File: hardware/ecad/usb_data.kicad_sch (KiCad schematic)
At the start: 4 parts, among them J6 Conn_01x04, U6 TS3USB30EDGSR

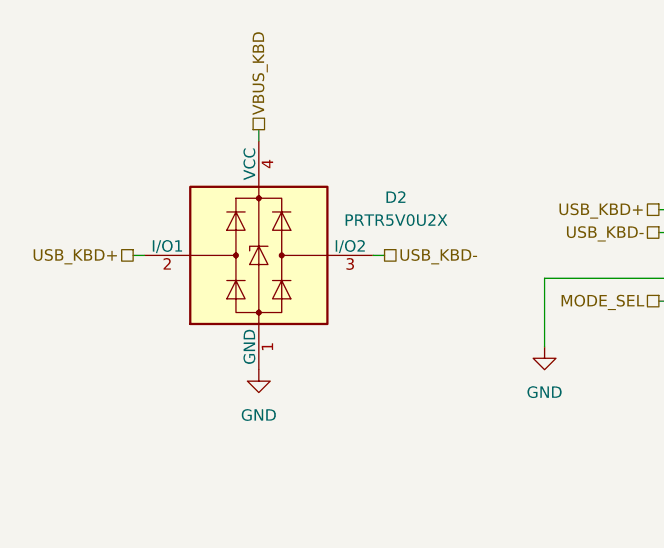
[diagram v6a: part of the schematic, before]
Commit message: Fixed minor errors and smaller issues withing schematics, moved v1 pcb and specific projet artifacts to archive. Updated changelog and finsihed pcb fopr version 2
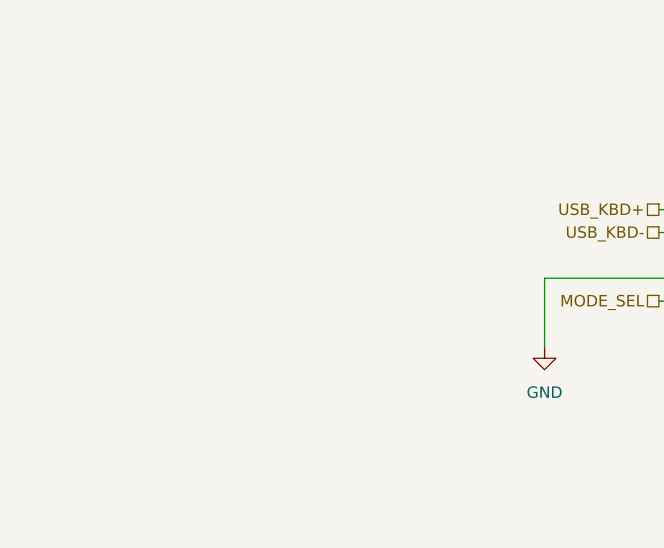
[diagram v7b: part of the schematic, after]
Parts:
- removed D2: PRTR5V0U2X, Package_TO_SOT_SMD:SOT-143, symbol Power_Protection:PRTR5V0U2X
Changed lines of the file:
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@@
-	(wire
-		(pts
-			(xy 99.06 101.6) (xy 100.33 101.6)
-		)
-		(stroke
-			(width 0)
-			(type default)
-		)
-	)
-	(wire
-		(pts
-			(xy 113.03 88.9) (xy 113.03 87.63)
-		)
-		(stroke
-			(width 0)
-			(type default)
-		)
-	)
 	(wire
 		(pts
@@
 		(pts
 			(xy 179.07 99.06) (xy 180.34 99.06)
-		)
-		(stroke
-			(width 0)
-			(type default)
-		)
-	)
-	(wire
-		(pts
-			(xy 125.73 101.6) (xy 127 101.6)
 		)
 		(stroke
@@
 		)
 	)
+	(hierarchical_label "USB_KBD+"
+		(shape passive)
+		(at 157.48 96.52 180)
+		(effects
+			(font
+				(size 1.27 1.27)
+			)
+			(justify right)
+		)
+	)
 	(hierarchical_label "USB_KBD-"
 		(shape passive)
-		(at 127 101.6 0)
-		(effects
-			(font
-				(size 1.27 1.27)
-			)
-			(justify left)
-		)
-	)
-	(hierarchical_label "USB_KBD+"
-		(shape passive)
-		(at 157.48 96.52 180)
+		(at 157.48 99.06 180)
 		(effects
 			(font
@@
 		)
 	)
-	(hierarchical_label "USB_KBD-"
-		(shape passive)
-		(at 157.48 99.06 180)
-		(effects
-			(font
-				(size 1.27 1.27)
-			)
-			(justify right)
-		)
-	)
-	(hierarchical_label "USB_KBD+"
-		(shape passive)
-		(at 99.06 101.6 180)
-		(effects
-			(font
-				(size 1.27 1.27)
-			)
-			(justify right)
-		)
-	)
 	(hierarchical_label "USB_ESP+"
 		(shape passive)
 		(at 180.34 96.52 0)
-		(effects
-			(font
-				(size 1.27 1.27)
-			)
-			(justify left)
-		)
-	)
-	(hierarchical_label "VBUS_KBD"
-		(shape passive)
-		(at 113.03 87.63 90)
 		(effects
 			(font
@@
 	)
 	(symbol
-		(lib_id "Power_Protection:PRTR5V0U2X")
-		(at 113.03 101.6 0)
-		(unit 1)
-		(body_style 1)
-		(exclude_from_sim no)
-		(in_bom yes)
-		(on_board yes)
-		(in_pos_files yes)
-		(dnp no)
-		(fields_autoplaced yes)
-		(property "Reference" "D2"
-			(at 128.27 95.1798 0)
-			(show_name no)
-			(do_not_autoplace no)
-			(effects
-				(font
-					(size 1.27 1.27)
-				)
-			)
-		)
-		(property "Value" "PRTR5V0U2X"
-			(at 128.27 97.7198 0)
-			(show_name no)
-			(do_not_autoplace no)
-			(effects
-				(font
-					(size 1.27 1.27)
-				)
-			)
-		)
-		(property "Footprint" "Package_TO_SOT_SMD:SOT-143"
-			(at 114.554 101.6 0)
-			(hide yes)
-			(show_name no)
-			(do_not_autoplace no)
-			(effects
-				(font
-					(size 1.27 1.27)
-				)
-			)
-		)
-		(property "Datasheet" "https://assets.nexperia.com/documents/data-sheet/PRTR5V0U2X.pdf"
-			(at 114.554 101.6 0)
-			(hide yes)
-			(show_name no)
-			(do_not_autoplace no)
-			(effects
-				(font
-					(size 1.27 1.27)
-				)
-			)
-		)
-		(property "Description" "Ultra low capacitance double rail-to-rail ESD protection diode, SOT-143"
-			(at 113.03 101.6 0)
-			(hide yes)
-			(show_name no)
-			(do_not_autoplace no)
-			(effects
-				(font
-					(size 1.27 1.27)
-				)
-			)
-		)
-		(pin "2"
-		)
-		(pin "4"
-		)
-		(pin "1"
-		)
-		(pin "3"
-		)
-		(instances
-			(project "midi2BLE"
-				(path "/1637d879-66a9-4939-ab4a-2374b8e6eb1f/2f8b77a8-0db6-4e3f-8b84-0f637a052a19"
-					(reference "D2")
-					(unit 1)
-				)
-			)
-		)
-	)
-	(symbol
 		(lib_id "Connector_Generic:Conn_01x04")
 		(at 257.81 93.98 0)
@@
 					(unit 1)
 				)
-			)
-		)
-	)
-	(symbol
-		(lib_id "power:GND")
-		(at 113.03 114.3 0)
-		(unit 1)
-		(body_style 1)
-		(exclude_from_sim no)
-		(in_bom yes)
-		(on_board yes)
-		(in_pos_files yes)
-		(dnp no)
-		(fields_autoplaced yes)
-		(property "Reference" "#PWR037"
-			(at 113.03 120.65 0)
-			(hide yes)
-			(show_name no)
-			(do_not_autoplace no)
-			(effects
-				(font
-					(size 1.27 1.27)
-				)
-			)
-		)
-		(property "Value" "GND"
-			(at 113.03 119.38 0)
-			(show_name no)
-			(do_not_autoplace no)
-			(effects
-				(font
-					(size 1.27 1.27)
-				)
-			)
-		)
-		(property "Footprint" ""
-			(at 113.03 114.3 0)
-			(hide yes)
-			(show_name no)
-			(do_not_autoplace no)
-			(effects
-				(font
-					(size 1.27 1.27)
-				)
-			)
-		)
-		(property "Datasheet" ""
-			(at 113.03 114.3 0)
-			(hide yes)
-			(show_name no)
-			(do_not_autoplace no)
-			(effects
-				(font
-					(size 1.27 1.27)
-				)
-			)
-		)
-		(property "Description" "Power symbol creates a global label with name \"GND\" , ground"
-			(at 113.03 114.3 0)
-			(hide yes)
-			(show_name no)
-			(do_not_autoplace no)
-			(effects
-				(font
-					(size 1.27 1.27)
-				)
-			)
-		)
-		(pin "1"
-		)
-		(instances
-			(project "midi2BLE"
-				(path "/1637d879-66a9-4939-ab4a-2374b8e6eb1f/2f8b77a8-0db6-4e3f-8b84-0f637a052a19"
-					(reference "#PWR037")
-					(unit 1)
-				)
